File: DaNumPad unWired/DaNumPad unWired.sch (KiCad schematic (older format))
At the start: 36 parts, among them J1 USB_C_Receptacle_USB2.0, J2 Conn_01x02, J3 Conn_01x04, Q1 SI2301CDS-T1-GE3, SW24 TS-A002, U1 SRV05-4, U2 nRF52840_holyiot_18010, U3 TP4056, U4 XC6206PxxxMR-Regulator_Linear

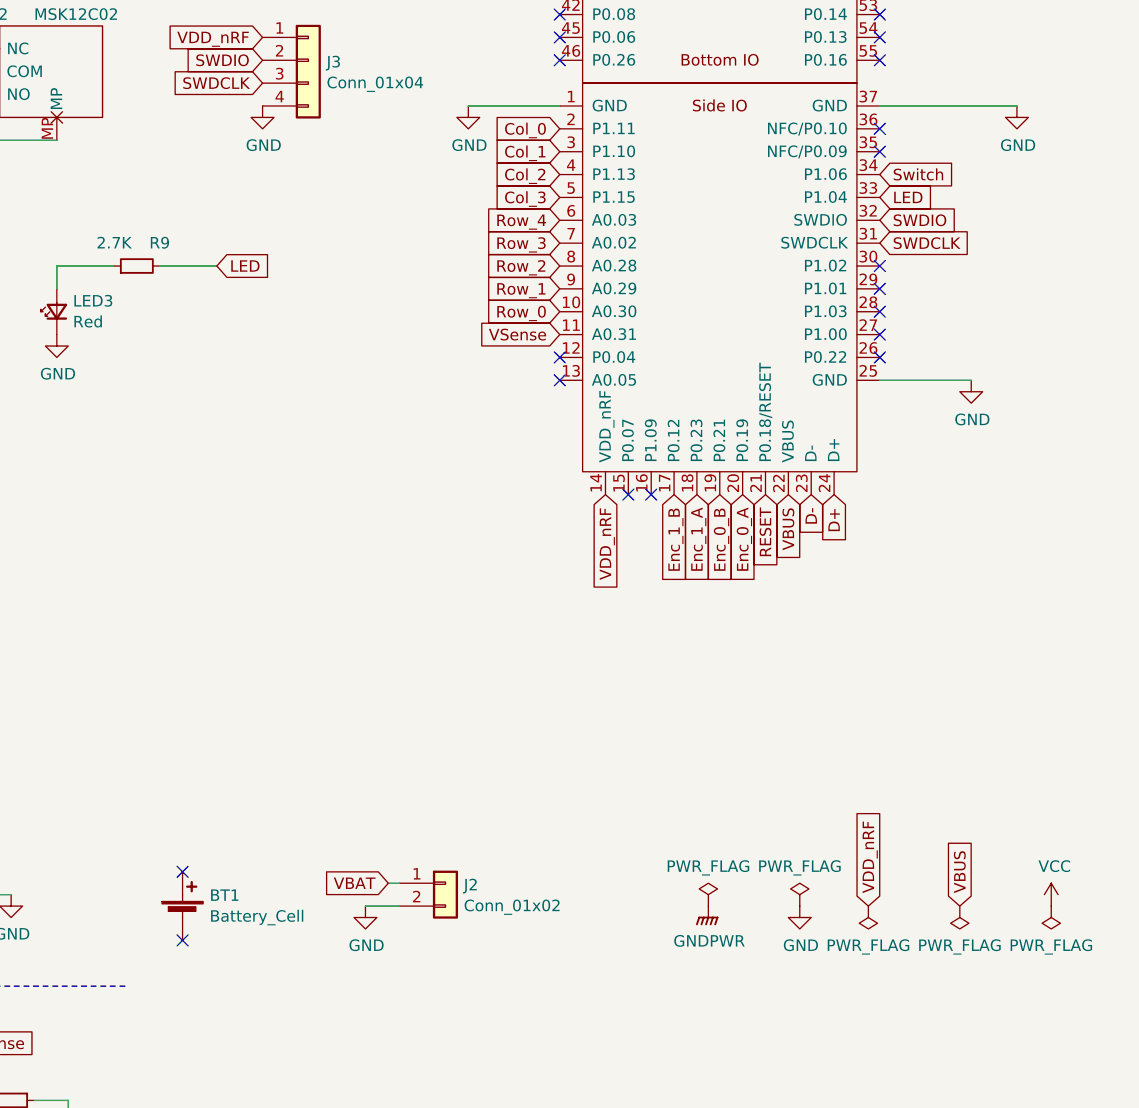
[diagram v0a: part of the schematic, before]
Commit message: Added silkscreen and PCB Plates
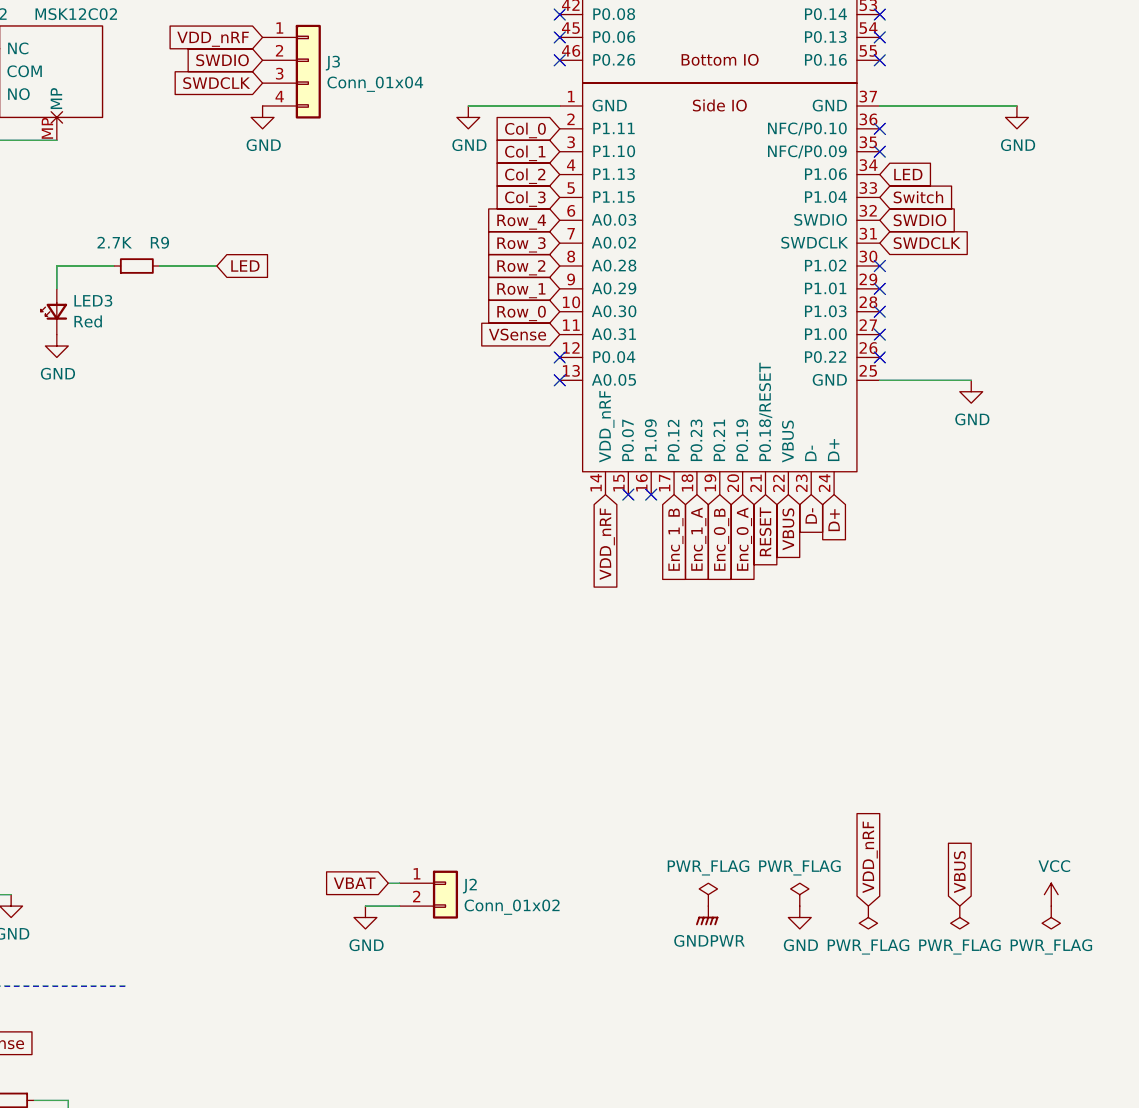
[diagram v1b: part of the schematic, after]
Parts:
- removed BT1: Battery_Cell, Keyboard Library:Lipo_battery_501528_1S_150mAh, symbol Device:Battery_Cell
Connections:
- net LED: now also U2.34 (P1.06); no longer U2.33 (P1.04)
- net Switch: now also U2.33 (P1.04); no longer U2.34 (P1.06)
- no-connect marks 34 -> 32
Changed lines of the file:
@@
 encoding utf-8
 Sheet 1 2
-Title ""
-Date ""
-Rev ""
-Comp ""
-Comment1 ""
-Comment2 ""
+Title "DaNumPad unWired"
+Date "2021-08-25"
+Rev "v1.00"
+Comp "Markus Knutsson <markus.knutsson@tweety.se>"
+Comment1 "https://github.com/TweetyDaBird"
+Comment2 "Licensed under CERN-OHL-S v2 or superseding version"
 Comment3 ""
 Comment4 ""
@@
 NoConn ~ 8750 3800
 NoConn ~ 8750 3900
-$Comp
-L Device:Battery_Cell BT1
-U 1 1 61870F7F
-P 7100 6250
-F 0 "BT1" H 7218 6346 50  0000 L CNN
-F 1 "Battery_Cell" H 7218 6255 50  0000 L CNN
-F 2 "Keyboard Library:Lipo_battery_501528_1S_150mAh" V 7100 6310 50  0001 C CNN
-F 3 "~" V 7100 6310 50  0001 C CNN
-	1    7100 6250
-	1    0    0    -1
-$EndComp
 Wire Wire Line
 	1250 2600 1250 2850
@@
 	6550 2850 6050 2850
 Connection ~ 6050 2850
-Text GLabel 10150 3000 2    50   Input ~ 0
+Text GLabel 10150 3100 2    50   Input ~ 0
 Switch
 Text GLabel 6200 2550 0    50   Input ~ 0
@@
 Wire Wire Line
 	7000 3400 7250 3400
-Text GLabel 10150 3100 2    50   Input ~ 0
+Text GLabel 10150 3000 2    50   Input ~ 0
 LED
 Text GLabel 7250 3400 2    50   Input ~ 0
@@
 	-1   0    0    1
 $EndComp
-NoConn ~ 7100 6050
-NoConn ~ 7100 6350
 $Comp
 L power:VCC #PWR0108
